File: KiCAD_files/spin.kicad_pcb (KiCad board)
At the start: 4 copper layers, 21 x 51 mm, 130 parts, among them J1 OwnTech_SPIN, J5 FTSH-107-01-F-DV-K, J6 USB_C_Receptacle_USB2.0, SW1 Push Button, SW2 Push Button, T1 Tab, T2 Tab, T3 Tab, T4 Tab, U1 STM32G474RE, U2 AZ1117-33, U3 WE-TVS-82400102, Y1 ECS-240-8-37-CKM-TR3 - 24MHz

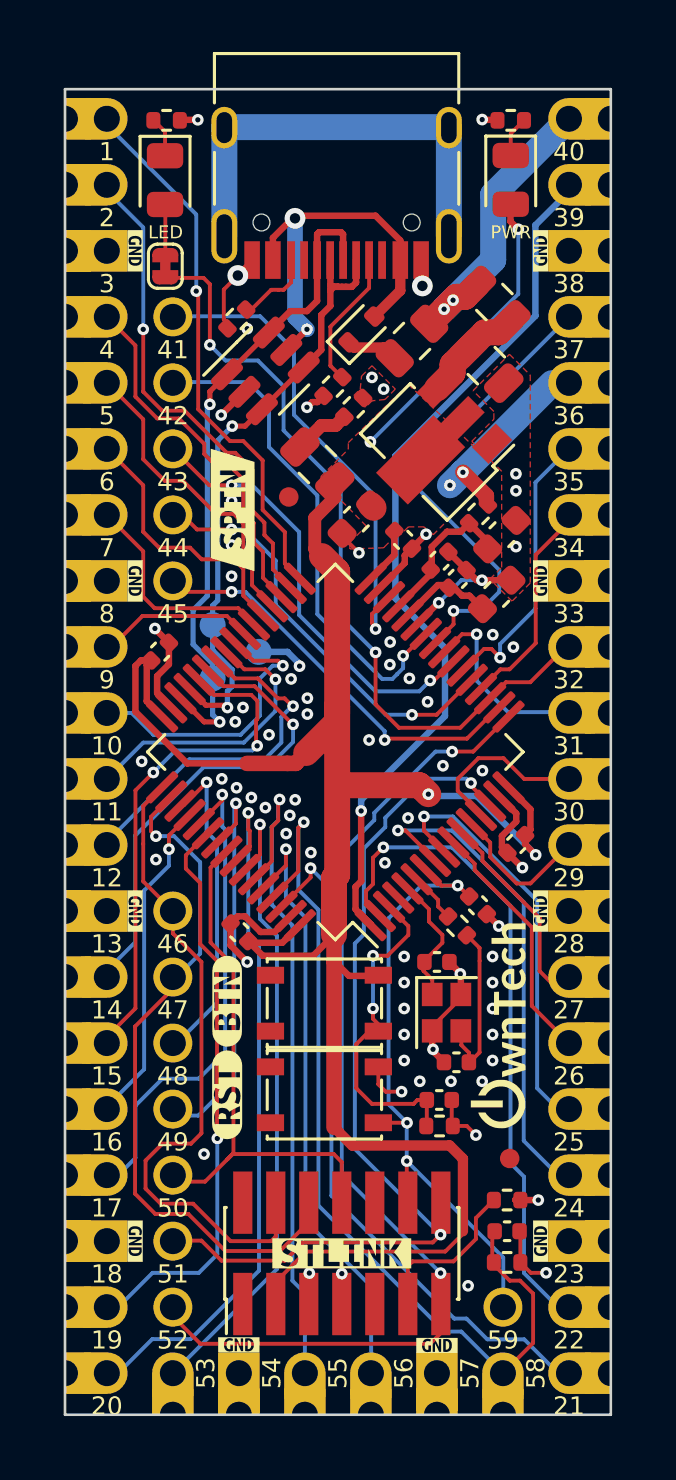
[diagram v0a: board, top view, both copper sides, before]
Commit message: Minor SPIN revision, bumping to v1.2.1 - Silkscreen improvements.
Signed-off-by: Jean Alinei <jean.alinei@owntech.org>
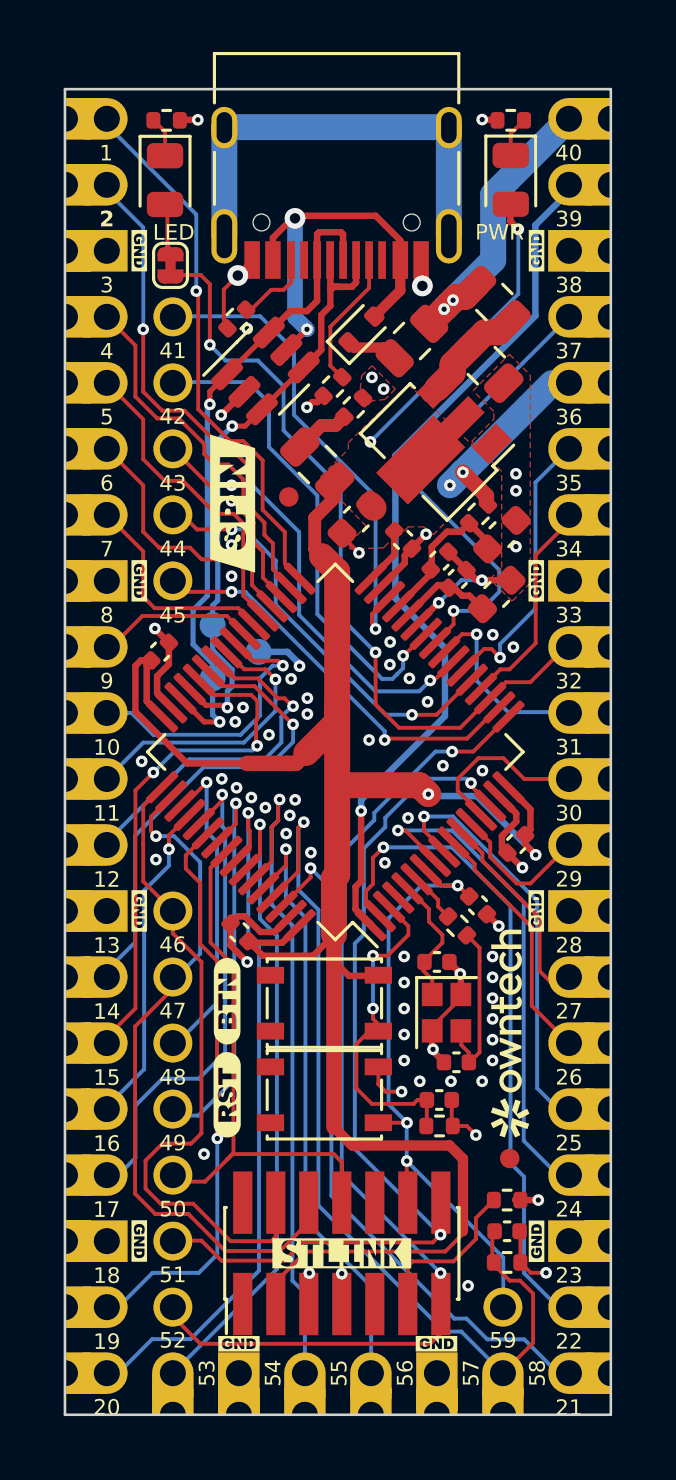
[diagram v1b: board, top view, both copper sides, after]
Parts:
- removed the G*** at (105.1, 64.9)
- removed the G*** at (98.9, 53.6)
- removed the REF** at (98.9, 33.5)
- removed kibuzzard-62C86250: G***, kibuzzard-62C86250
- removed kibuzzard-62C86302: G***, kibuzzard-62C86302
- removed kibuzzard-62C8630E: G***, kibuzzard-62C8630E
- removed kibuzzard-62C86324: G***, kibuzzard-62C86324
- removed kibuzzard-62C8632C: G***, kibuzzard-62C8632C
- removed kibuzzard-62C86335: G***, kibuzzard-62C86335
- removed kibuzzard-62C8633C: G***, kibuzzard-62C8633C
- removed kibuzzard-62C86349: G***, kibuzzard-62C86349
- removed kibuzzard-62C86353: G***, kibuzzard-62C86353
- removed kibuzzard-62C8635A: G***, kibuzzard-62C8635A
- removed kibuzzard-62C86362: G***, kibuzzard-62C86362
- removed kibuzzard-62C8636A: G***, kibuzzard-62C8636A
- removed kibuzzard-62C86371: G***, kibuzzard-62C86371
- removed kibuzzard-62C8637B: G***, kibuzzard-62C8637B
- removed kibuzzard-62C86384: G***, kibuzzard-62C86384
- removed kibuzzard-62C8639B: G***, kibuzzard-62C8639B
- removed kibuzzard-62C863A5: G***, kibuzzard-62C863A5
- removed kibuzzard-62C863AC: G***, kibuzzard-62C863AC
- removed kibuzzard-62C863B3: G***, kibuzzard-62C863B3
- removed kibuzzard-62C863BD: G***, kibuzzard-62C863BD
- removed kibuzzard-62C863C4: G***, kibuzzard-62C863C4
- removed kibuzzard-62C863D6: G***, kibuzzard-62C863D6
- removed kibuzzard-62C863DD: G***, kibuzzard-62C863DD
- removed kibuzzard-62C863E7: G***, kibuzzard-62C863E7
- removed kibuzzard-62C863ED: G***, kibuzzard-62C863ED
- removed kibuzzard-62C863F3: G***, kibuzzard-62C863F3
- removed kibuzzard-62C863FB: G***, kibuzzard-62C863FB
- removed kibuzzard-62C86401: G***, kibuzzard-62C86401
- removed kibuzzard-62C86407: G***, kibuzzard-62C86407
- removed kibuzzard-62C8640E: G***, kibuzzard-62C8640E
- removed kibuzzard-62C86415: G***, kibuzzard-62C86415
- removed kibuzzard-62C8641D: G***, kibuzzard-62C8641D
- removed kibuzzard-62C86424: G***, kibuzzard-62C86424
- removed kibuzzard-62C8642B: G***, kibuzzard-62C8642B
- removed kibuzzard-62C86431: G***, kibuzzard-62C86431
- removed kibuzzard-62C86437: G***, kibuzzard-62C86437
- removed kibuzzard-62C8643D: G***, kibuzzard-62C8643D
- removed kibuzzard-62C86450: G***, kibuzzard-62C86450
- removed kibuzzard-62C86458: G***, kibuzzard-62C86458
- removed kibuzzard-62C86461: G***, kibuzzard-62C86461
- removed kibuzzard-62C86468: G***, kibuzzard-62C86468
- removed kibuzzard-62C86470: G***, kibuzzard-62C86470
- removed kibuzzard-62C864F6: G***, kibuzzard-62C864F6
- removed kibuzzard-62C86A6F: G***, kibuzzard-62C86A6F
- removed kibuzzard-62C86A9B: G***, kibuzzard-62C86A9B
- removed kibuzzard-62C86AAB: G***, kibuzzard-62C86AAB
- removed kibuzzard-62C86AB2: G***, kibuzzard-62C86AB2
- removed kibuzzard-62C86ABB: G***, kibuzzard-62C86ABB
- removed kibuzzard-62C86AC0: G***, kibuzzard-62C86AC0
- removed kibuzzard-641CBEFD: G***, kibuzzard-641CBEFD
- removed kibuzzard-648744C7: G***, kibuzzard-648744C7
- removed kibuzzard-657B112C (x10): G***, kibuzzard-657B112C
- removed kibuzzard-657B1770 (x8): G***, kibuzzard-657B1770
- removed kibuzzard-657B2823 (x3): G***, kibuzzard-657B2823
- removed kibuzzard-657B2A3E: G***, kibuzzard-657B2A3E
- removed kibuzzard-657C3BD1: G***, kibuzzard-657C3BD1
- removed kibuzzard-657C3BE0: G***, kibuzzard-657C3BE0
- removed kibuzzard-6687F07D: G***, kibuzzard-6687F07D
- added G***: LOGO, Footprints:compo_pos_vertical7-5, B.Cu at (98.8, 33.2)
- added G1: LOGO, Footprints:owntech_mini8, F.Cu at (105.5, 65.2)
- added kibuzzard-68DA5684: G***, kibuzzard-68DA5684, F.Cu at (94.6, 64.0)
- added kibuzzard-68DA56F7: G***, kibuzzard-68DA56F7, F.Cu at (94.6, 67.5)
- added kibuzzard-68DA5768: G***, kibuzzard-68DA5768, F.Cu at (106.5, 35.1)
- added kibuzzard-68DA5768: G***, kibuzzard-68DA5768, F.Cu at (106.5, 47.8)
- added kibuzzard-68DA57E1: G***, kibuzzard-68DA57E1, F.Cu at (91.2, 73.2)
- added kibuzzard-68DA57E1: G***, kibuzzard-68DA57E1, F.Cu at (91.2, 35.1)
- added kibuzzard-68DA57E1: G***, kibuzzard-68DA57E1, F.Cu at (102.7, 77.1)
- added kibuzzard-68DA57E1: G***, kibuzzard-68DA57E1, F.Cu at (106.5, 73.2)
- added kibuzzard-68DA57E1: G***, kibuzzard-68DA57E1, F.Cu at (106.5, 60.5)
- added kibuzzard-68DA57E1: G***, kibuzzard-68DA57E1, F.Cu at (91.2, 47.8)
- added kibuzzard-68DA57E1: G***, kibuzzard-68DA57E1, F.Cu at (95.1, 77.1)
- added kibuzzard-68DA57E1: G***, kibuzzard-68DA57E1, F.Cu at (91.2, 60.5)
- added kibuzzard-68DA61DB: G***, kibuzzard-68DA61DB, B.Cu at (105.4, 47.8)
- added kibuzzard-68DA61DB: G***, kibuzzard-68DA61DB, B.Cu at (94.9, 73.2)
- added kibuzzard-68DA61DB: G***, kibuzzard-68DA61DB, B.Cu at (105.4, 35.1)
- added kibuzzard-68DA61DB: G***, kibuzzard-68DA61DB, B.Cu at (94.9, 60.5)
- added kibuzzard-68DA61DB: G***, kibuzzard-68DA61DB, B.Cu at (92.4, 35.1)
- added kibuzzard-68DA61DB: G***, kibuzzard-68DA61DB, B.Cu at (105.4, 60.5)
- added kibuzzard-68DA61DB: G***, kibuzzard-68DA61DB, B.Cu at (105.4, 72.6)
- added kibuzzard-68DA61DB: G***, kibuzzard-68DA61DB, B.Cu at (94.9, 47.8)
- added kibuzzard-68DA61F7: G***, kibuzzard-68DA61F7, B.Cu at (94.9, 37.6)
- added kibuzzard-68DA621E: G***, kibuzzard-68DA621E, B.Cu at (97.9, 37.6)
- added kibuzzard-68DA6234: G***, kibuzzard-68DA6234, B.Cu at (94.9, 40.2)
- added kibuzzard-68DA6241: G***, kibuzzard-68DA6241, B.Cu at (97.5, 40.2)
- added kibuzzard-68DA6253: G***, kibuzzard-68DA6253, B.Cu at (94.9, 42.7)
- added kibuzzard-68DA6266: G***, kibuzzard-68DA6266, B.Cu at (97.6, 42.7)
- added kibuzzard-68DA627F: G***, kibuzzard-68DA627F, B.Cu at (97.6, 45.2)
- added kibuzzard-68DA628C: G***, kibuzzard-68DA628C, B.Cu at (97.6, 47.8)
- added kibuzzard-68DA62C4: G***, kibuzzard-68DA62C4, B.Cu at (92.0, 50.3)
- added kibuzzard-68DA62D2: G***, kibuzzard-68DA62D2, B.Cu at (92.0, 52.9)
- added kibuzzard-68DA62DF: G***, kibuzzard-68DA62DF, B.Cu at (92.0, 55.4)
- added kibuzzard-68DA62EF: G***, kibuzzard-68DA62EF, B.Cu at (92.1, 57.9)
- added kibuzzard-68DA6304: G***, kibuzzard-68DA6304, B.Cu at (105.8, 45.2)
- added kibuzzard-68DA630F: G***, kibuzzard-68DA630F, B.Cu at (105.8, 42.7)
- added kibuzzard-68DA631E: G***, kibuzzard-68DA631E, B.Cu at (105.9, 37.6)
- added kibuzzard-68DA6335: G***, kibuzzard-68DA6335, B.Cu at (105.0, 32.5)
- added kibuzzard-68DA6341: G***, kibuzzard-68DA6341, B.Cu at (105.7, 30.0)
- added kibuzzard-68DA634D: G***, kibuzzard-68DA634D, B.Cu at (105.4, 40.2)
- added kibuzzard-68DA636F: G***, kibuzzard-68DA636F, B.Cu at (105.8, 50.3)
- added kibuzzard-68DA6374: G***, kibuzzard-68DA6374, B.Cu at (105.8, 52.9)
- added kibuzzard-68DA6386: G***, kibuzzard-68DA6386, B.Cu at (105.8, 55.4)
- added kibuzzard-68DA6390: G***, kibuzzard-68DA6390, B.Cu at (105.8, 57.9)
- added kibuzzard-68DA63D4: G***, kibuzzard-68DA63D4, B.Cu at (105.8, 63.0)
- added kibuzzard-68DA63E1: G***, kibuzzard-68DA63E1, B.Cu at (105.8, 65.6)
- added kibuzzard-68DA63ED: G***, kibuzzard-68DA63ED, B.Cu at (105.9, 68.1)
- added kibuzzard-68DA63F9: G***, kibuzzard-68DA63F9, B.Cu at (105.8, 70.6)
- added kibuzzard-68DA6416: G***, kibuzzard-68DA6416, B.Cu at (105.4, 74.1)
- added kibuzzard-68DA643B: G***, kibuzzard-68DA643B, B.Cu at (103.0, 75.7)
- added kibuzzard-68DA6452: G***, kibuzzard-68DA6452, B.Cu at (97.6, 75.7)
- added kibuzzard-68DA645C: G***, kibuzzard-68DA645C, B.Cu at (94.9, 75.7)
- added kibuzzard-68DA6470: G***, kibuzzard-68DA6470, B.Cu at (98.0, 60.5)
- added kibuzzard-68DA6496: G***, kibuzzard-68DA6496, B.Cu at (98.0, 63.0)
- added kibuzzard-68DA64A4: G***, kibuzzard-68DA64A4, B.Cu at (94.9, 65.6)
- added kibuzzard-68DA64AE: G***, kibuzzard-68DA64AE, B.Cu at (98.0, 65.6)
- added kibuzzard-68DA64B9: G***, kibuzzard-68DA64B9, B.Cu at (94.9, 68.1)
- added kibuzzard-68DA64C2: G***, kibuzzard-68DA64C2, B.Cu at (97.5, 68.1)
- added kibuzzard-68DA64DC: G***, kibuzzard-68DA64DC, B.Cu at (97.5, 70.6)
- added kibuzzard-68DA64F4: G***, kibuzzard-68DA64F4, B.Cu at (97.6, 73.2)
- added kibuzzard-68DA6750: G***, kibuzzard-68DA6750, B.Cu at (91.0, 77.3)
- added kibuzzard-68DA6783: G***, kibuzzard-68DA6783, B.Cu at (92.6, 76.9)
- added kibuzzard-68DA679F: G***, kibuzzard-68DA679F, B.Cu at (102.7, 76.9)
- added kibuzzard-68DA679F: G***, kibuzzard-68DA679F, B.Cu at (95.1, 76.9)
- added kibuzzard-68DA67AE: G***, kibuzzard-68DA67AE, B.Cu at (97.6, 76.9)
- added kibuzzard-68DA67BA: G***, kibuzzard-68DA67BA, B.Cu at (100.2, 77.0)
- added kibuzzard-68DA67CE: G***, kibuzzard-68DA67CE, B.Cu at (105.2, 76.9)
- added kibuzzard-68DA67E1: G***, kibuzzard-68DA67E1, B.Cu at (106.7, 77.3)
- added kibuzzard-68DA6850: G***, kibuzzard-68DA6850, B.Cu at (97.5, 51.8)
- added kibuzzard-68DA685D: G***, kibuzzard-68DA685D, B.Cu at (97.9, 50.5)
- added kibuzzard-68DA687C: G***, kibuzzard-68DA687C, B.Cu at (97.4, 49.3)
- added kibuzzard-68DA9FF6: G***, kibuzzard-68DA9FF6, B.Cu at (99.3, 55.4)
- added kibuzzard-68DAA085: G***, kibuzzard-68DAA085, F.Cu at (94.8, 44.8)
- added kibuzzard-68DAA3CB: G***, kibuzzard-68DAA3CB, B.Cu at (92.4, 32.5)
- added kibuzzard-68DAA3D4: G***, kibuzzard-68DAA3D4, B.Cu at (92.3, 30.0)
- added kibuzzard-68DAA579: G***, kibuzzard-68DAA579, B.Cu at (94.8, 70.6)
- added kibuzzard-68DAA5C2: G***, kibuzzard-68DAA5C2, B.Cu at (94.8, 45.2)
- added kibuzzard-68DAA604: G***, kibuzzard-68DAA604, B.Cu at (94.8, 63.0)
- J5: value FTSH-107-01-F-DV-K -> FTSH-107-01-F-DV-K
- moved JP1 0.20 mm to (92.5, 35.6)
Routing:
- net GNDD: vias 74 -> 75
